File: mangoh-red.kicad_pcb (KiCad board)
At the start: 6 copper layers, 70 x 61.8 mm, 533 parts, among them CN1000 uFL, CN301 uFL, CN302 uFL, CN303 uFL, CN304 USB_A, CN305 USB_B_Micro, CN306 Conn_02x19_Counter_Clockwise, CN307 Conn_02x13_Odd_Even, CN310 Conn_02x03_Odd_Even, CN312 Conn_02x03_Odd_Even, CN500 JP036-RT3B4AB, CN801 USB_B_Micro, CN802 Conn_01x02, CN804 Conn_01x03, J200 CF3-Socket, SW401 Conn_02x08_Counter_Clockwise, U1000 MT7697, U1001 MX25L3233FM1I-08G_TR, U1004 SX1509BIULTRT, U1005 TPS61253YFFR, U1006 CP2130-F01-GM, U1007 24AA32AF-I-MNY, U1010 74LVC2G126HD4-7, U1020 74LVC2G126HD4-7, U301 FT230XQ-R, U302 TS3A5018RSVR, U304 74LVC2G126HD4-7, U306 FXMA108BQX, U307 FXMA108BQX, U337 FXMA108BQX, U400 NCP303LSN30T1G, U401 74AUP1G08GM, U402 74AUP1G08GM, U404 TCA9546APWR, U405 74AUP1G08GM, U500 WM8944BECS_R, U501 TS3A5018RSVR, U600 XC6223H29B9R-G, U610 TXS02612ZQSR, U701 USB3503A-1-GL-TR, U702 MIC2026-1YM, U704 BMI160, U705 BMP280, U706 PNJ4K01F, U800 BQ24296RGER, U801 LTC2942IDCB_TRMPBF, U900 TPS7A7300, U901 TPS62420DRC, U903 XC6221A182MR, Y1000 CT2520DB26000C0FZZA1

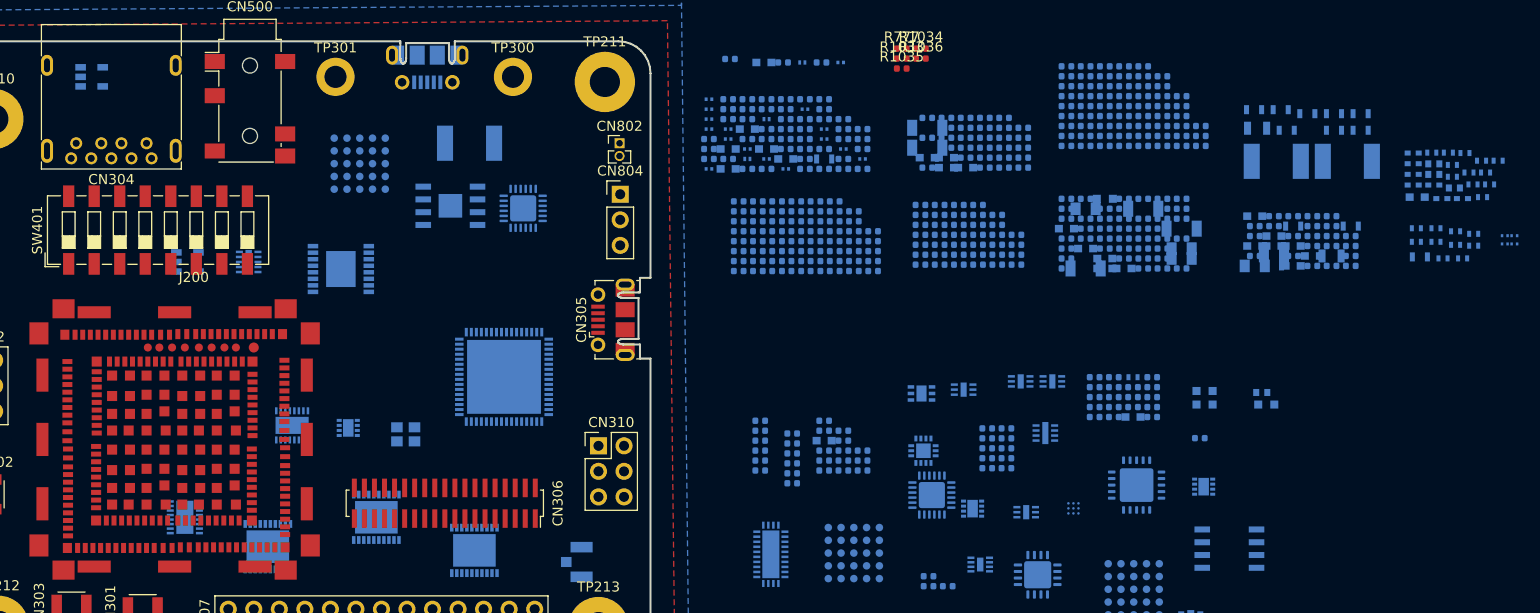
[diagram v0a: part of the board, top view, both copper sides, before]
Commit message: Refactor footprints and paths
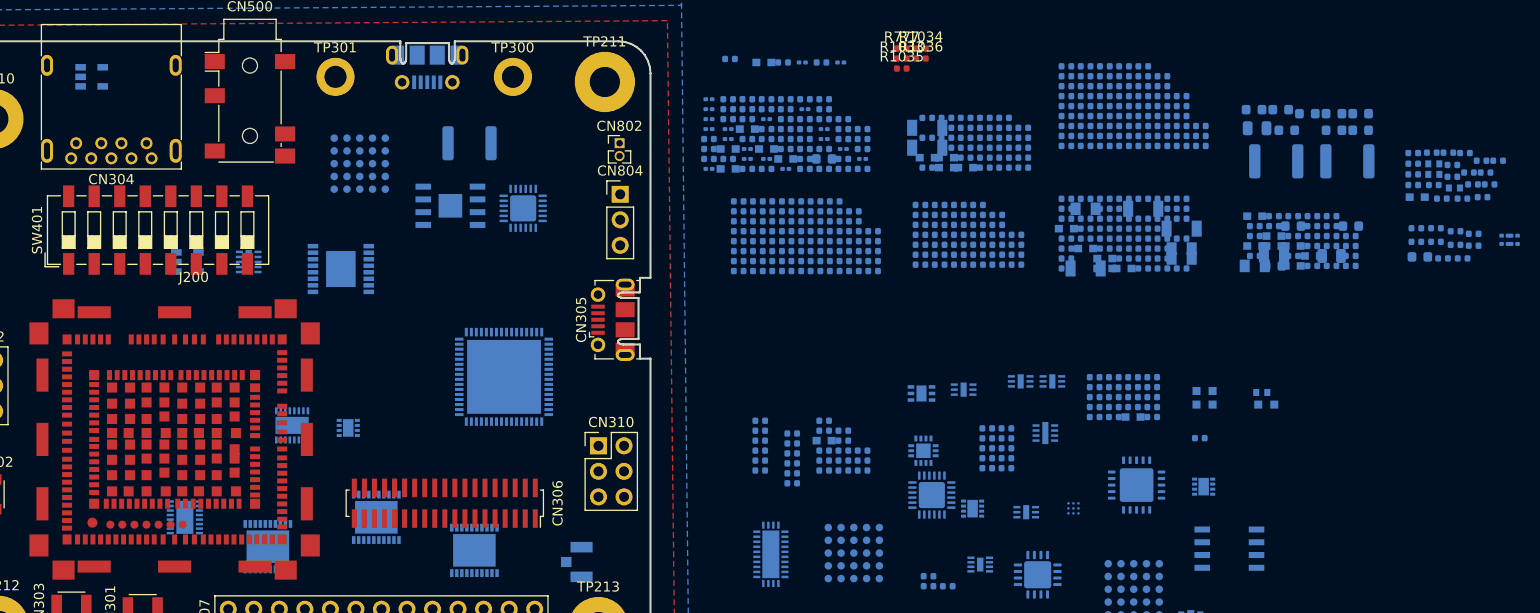
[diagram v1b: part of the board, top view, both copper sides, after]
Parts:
- removed Y1000: CT2520DB26000C0FZZA1, Crystal:Crystal_SMD_2520-4Pin_2.5x2.0mm
- C1005, C1010, C1013, C1022, C1023, C1024, C304, C308, C310, C311, C318, C515, C605, C801, C803, C807, C808, C809, C810, C818, C903, C924, C926, C927, C928: footprint Capacitors_SMD:C_0603 -> Capacitor_SMD:C_0603_1608Metric
- C1034, C1035, C1036, C1037, C1038, C1039, C1045, C1053, C1060, C1061, C1063, C1065, C1087, C1098, C1099, C1100: footprint Capacitors_SMD:C_0201 -> Capacitor_SMD:C_0201_0603Metric
- C302, C309, C908, C912, C920: footprint Capacitors_SMD:C_1206 -> Capacitor_SMD:C_1206_3216Metric
- C320, C321, C322, C355, C356, C360, C362: footprint Capacitors_SMD:C_0402 -> Capacitor_SMD:C_0402_1005Metric
- C800, C805, C906, C952, C955: footprint Capacitors_SMD:C_0805 -> Capacitor_SMD:C_0805_2012Metric
- C929: footprint LEDs:LED_0603 -> Capacitor_SMD:C_0402_1005Metric
- J200: footprint footprints:cf3 -> MangOH-Red:cf3
- L1001, L1002, L1026, L1087: footprint Inductors_SMD:L_0201 -> Inductor_SMD:L_0201_0603Metric
- L300, L500, L501, L502, L503, L504, L505, L506, L507: footprint Inductors_SMD:L_0402 -> Inductor_SMD:L_0402_1005Metric
- L508, L900, L901, L902, L903, L906, L907, L910, L912: footprint Inductors_SMD:L_0603 -> Inductor_SMD:L_0603_1608Metric
- L802, L904, L905: footprint Inductors_SMD:L_1812 -> Inductor_SMD:L_1812_4532Metric
- L911: footprint Inductors_SMD:L_0805 -> Inductor_SMD:L_0805_2012Metric
- R1006, R820, R826, R827: footprint Resistors_SMD:R_0603 -> Resistor_SMD:R_0603_1608Metric
- R1071, R1087, R1098: footprint Resistors_SMD:R_0201 -> Resistor_SMD:R_0201_0603Metric
- R310, R311, R312, R313, R340, R341, R343, R347, R361, R372, R378, R505, R506, R507: footprint Resistors_SMD:R_0402 -> Resistor_SMD:R_0402_1005Metric
- R828: footprint Resistors_SMD:R_0805 -> Resistor_SMD:R_0805_2012Metric

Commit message: Updates
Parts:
- added TP1000: TestPoint, MangOH-Red:Test_Point_Pad_d_0100, F.Cu at (269.6, 92.0)
- added TP1001: TestPoint, MangOH-Red:Test_Point_Pad_d_0100, F.Cu at (269.6, 89.9)
- added TP1002: TestPoint, MangOH-Red:Test_Point_Pad_d_0100, F.Cu at (267.5, 92.0)
- added TP1003: TestPoint, MangOH-Red:Test_Point_Pad_d_0100, F.Cu at (267.5, 89.9)
- added TP1004: TestPoint, MangOH-Red:Test_Point_Pad_d_0100, F.Cu at (265.5, 92.0)
- added TP1021: TestPoint, MangOH-Red:Test_Point_Pad_d_0100, F.Cu at (265.5, 89.9)
- added TP1022: TestPoint, MangOH-Red:Test_Point_Pad_d_0100, F.Cu at (263.4, 92.0)
- added TP1023: TestPoint, MangOH-Red:Test_Point_Pad_d_0100, F.Cu at (263.4, 89.9)
- added TP1024: TestPoint, MangOH-Red:Test_Point_Pad_d_0100, F.Cu at (261.4, 92.0)
- added TP1025: TestPoint, MangOH-Red:Test_Point_Pad_d_0100, F.Cu at (261.4, 89.9)
- added TP224: TestPoint, MangOH-Red:Test_Point_Pad_d_0100, F.Cu at (267.5, 98.8)
- added TP225: TestPoint, MangOH-Red:Test_Point_Pad_d_0100, F.Cu at (261.4, 98.8)
- added TP227: TestPoint, MangOH-Red:Test_Point_Pad_d_0100, F.Cu at (261.4, 100.9)
- added TP228: TestPoint, MangOH-Red:Test_Point_Pad_d_0100, F.Cu at (263.4, 98.8)
- added TP230: TestPoint, MangOH-Red:Test_Point_Pad_d_0100, F.Cu at (263.4, 100.9)
- added TP232: TestPoint, MangOH-Red:Test_Point_Pad_d_0100, F.Cu at (265.5, 98.8)
- added TP261: TestPoint, MangOH-Red:Test_Point_Pad_d_0100, F.Cu at (265.5, 100.9)
- added TP324: TestPoint, MangOH-Red:Test_Point_Pad_d_0100, F.Cu at (273.1, 98.8)
- added TP325: TestPoint, MangOH-Red:Test_Point_Pad_d_0100, F.Cu at (273.1, 100.9)
- added TP327: TestPoint, MangOH-Red:Test_Point_Pad_d_0100, F.Cu at (275.2, 98.8)
- added TP328: TestPoint, MangOH-Red:Test_Point_Pad_d_0100, F.Cu at (275.2, 100.9)
- added TP500: TestPoint, MangOH-Red:Test_Point_Pad_d_0035, F.Cu at (282.9, 96.6)
- added TP802: TestPoint, MangOH-Red:Test_Point_Pad_d_0100, F.Cu at (276.9, 92.0)
- added TP803: TestPoint, MangOH-Red:Test_Point_Pad_d_0100, F.Cu at (276.9, 89.9)
- added TP804: TestPoint, MangOH-Red:Test_Point_Pad_d_0100, F.Cu at (278.9, 89.9)
- added TP805: TestPoint, MangOH-Red:Test_Point_Pad_d_0100, F.Cu at (274.8, 89.9)
- added TP806: TestPoint, MangOH-Red:Test_Point_Pad_d_0100, F.Cu at (274.8, 92.0)
- added TP901: TestPoint, MangOH-Red:Test_Point_Pad_d_0100, F.Cu at (285.3, 89.9)
- added TP906: TestPoint, MangOH-Red:Test_Point_Pad_d_0100, F.Cu at (285.3, 92.0)
- added TP907: TestPoint, MangOH-Red:Test_Point_Pad_d_0100, F.Cu at (287.3, 89.9)
- added TP910: TestPoint, MangOH-Red:Test_Point_Pad_d_0100, F.Cu at (287.3, 92.0)
- TP210, TP211, TP212, TP213: footprint MountingHole:MountingHole_3mm_Pad -> MangOH-Red:Test_Point_Pad_d_0650
- TP300: value IOT_Mounting_Point_1 -> TestPoint; footprint MountingHole:MountingHole_2.2mm_M2_DIN965_Pad -> MangOH-Red:Test_Point_Pad_d_0100
- TP301: value IOT_Mounting_Point_2 -> TestPoint; footprint MountingHole:MountingHole_2.2mm_M2_DIN965_Pad -> MangOH-Red:Test_Point_Pad_d_0100
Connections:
- C1100 pad 1: Net-(ANT1000-Pad3) -> (no net)
- C230 pad 1: W_DISABLE_N -> (no net)
- C301 pad 2: RF_GPS -> (no net)
- CN305 pad 4: Net-(CN305-Pad4) -> (no net)
- CN306 pad 16: SPI1_CLK -> (no net)
- CN306 pad 17: SPI1_MISO -> (no net)
- CN306 pad 18: SPI1_MOSI -> (no net)
- CN306 pad 31: CARD_DETECT_IOT0 -> (no net)
- CN500 pad 2: Net-(CN500-Pad2) -> (no net)
- CN500 pad 3: Net-(CN500-Pad3) -> (no net)
- CN801 pad 2: Net-(CN801-Pad2) -> (no net)
- CN801 pad 3: Net-(CN801-Pad3) -> (no net)
- D410 pad 1: Net-(D410-Pad1) -> (no net)
- R216 pad 2: Net-(J200-Pad23) -> (no net)
- R217 pad 2: Net-(J200-Pad22) -> (no net)
- R222 pad 2: Net-(D200-Pad2) -> (no net)
- R223 pad 1: Net-(J200-Pad99) -> (no net)
- R224 pad 1: Net-(J200-Pad98) -> (no net)
- R230 pad 2: Net-(J200-Pad25) -> (no net)
- R238 pad 1: Net-(J200-Pad45) -> (no net)
- R252 pad 1: Net-(J200-Pad91) -> (no net)
- R287 pad 2: Net-(R287-Pad2) -> (no net)
- R306 pad 2: BAT_RTC -> (no net)
- R343 pad 2: Net-(Q405-Pad2) -> (no net)
- R345 pad 1: Net-(J200-Pad1) -> (no net)
- R346 pad 1: Net-(J200-Pad66) -> (no net)
- R347 pad 2: Net-(Q312-Pad2) -> (no net)
- R413 pad 1: Net-(D401-Pad2) -> (no net)
- R435 pad 1: Net-(D402-Pad2) -> (no net)
- R600 pad 2: Net-(CN600-PadT5) -> (no net)
- R604 pad 2: UIM1_DATA -> (no net)
- R611 pad 1: UIM2_DATA -> (no net)
- R611 pad 2: Net-(R611-Pad2) -> (no net)
- R645 pad 1: Net-(R645-Pad1) -> (no net)
- R645 pad 2: UIM2_CLK -> (no net)
- SW401 pad 1: PWR_ON -> (no net)
- U1000 pad 1: Net-(U1000-Pad1) -> (no net)
- U1000 pad 40: Net-(L1000-Pad1) -> (no net)
- U1000 pad 58: Net-(U1000-Pad58) -> (no net)
- U1000 pad 61: Net-(U1000-Pad61) -> (no net)
- U1004 pad 11: Net-(U1004-Pad11) -> (no net)
- U1006 pad 10: Net-(U1006-Pad10) -> (no net)
- U1006 pad 11: Net-(U1006-Pad11) -> (no net)
- U1006 pad 12: Net-(U1006-Pad12) -> (no net)
- U1006 pad 13: Net-(U1006-Pad13) -> (no net)
- U1006 pad 14: Net-(U1006-Pad14) -> (no net)
- U1006 pad 15: Net-(U1006-Pad15) -> (no net)
- U1006 pad 17: Net-(U1006-Pad17) -> (no net)
- U1006 pad 18: Net-(U1006-Pad18) -> (no net)
- U301 pad 11: Net-(U301-Pad11) -> (no net)
- U301 pad 12: Net-(U301-Pad12) -> (no net)
- U301 pad 14: Net-(U301-Pad14) -> (no net)
- U301 pad 5: Net-(U301-Pad5) -> (no net)
- U302 pad 1: Net-(U302-Pad1) -> (no net)
- U302 pad 11: Net-(U302-Pad11) -> (no net)
- U306 pad 14: WP_GPIO_7_lvl -> (no net)
- U306 pad 16: Net-(U306-Pad16) -> (no net)
- U306 pad 2: WP_GPIO_3 -> (no net)
- U306 pad 3: WP_GPIO_1 -> (no net)
- U306 pad 5: Net-(U306-Pad5) -> (no net)
- U306 pad 6: WP_GPIO_8 -> (no net)
- U306 pad 7: WP_GPIO_7 -> (no net)
- U307 pad 16: Net-(U307-Pad16) -> (no net)
- U307 pad 5: Net-(U307-Pad5) -> (no net)
- U337 pad 11: Net-(Q405-Pad6) -> (no net)
- U337 pad 12: Net-(U337-Pad12) -> (no net)
- U337 pad 13: Net-(U337-Pad13) -> (no net)
- U337 pad 14: Net-(U337-Pad14) -> (no net)
- U337 pad 4: UART1_CTS -> (no net)
- U337 pad 7: Net-(U337-Pad7) -> (no net)
- U337 pad 8: Net-(U337-Pad8) -> (no net)
- U337 pad 9: Net-(U337-Pad9) -> (no net)
- U400 pad 4: Net-(U400-Pad4) -> (no net)
- U401 pad 5: Net-(U401-Pad5) -> (no net)
- U402 pad 5: Net-(U402-Pad5) -> (no net)
- U405 pad 5: Net-(U405-Pad5) -> (no net)
- U500 pad C5: Net-(U500-PadC5) -> (no net)
- U500 pad D4: Net-(U500-PadD4) -> (no net)
- U500 pad D5: Net-(U500-PadD5) -> (no net)
- U500 pad E5: Net-(U500-PadE5) -> (no net)
- U610 pad A1: SD_D2 -> (no net)
- U610 pad B1: SD_D3 -> (no net)
- U610 pad C1: SD_CMD -> (no net)
- U610 pad D1: SD_D0 -> (no net)
- U610 pad D2: SD_CLK -> (no net)
- U610 pad E1: SD_D1 -> (no net)
- U701 pad B3: Net-(OSC1000-Pad3) -> (no net)
- U701 pad C4: Net-(U701-PadC4) -> (no net)
- U701 pad E1: HSIC_STRB -> (no net)
- U701 pad E2: HSIC_DATA -> (no net)
- U704 pad 10: Net-(U704-Pad10) -> (no net)
- U704 pad 11: Net-(U704-Pad11) -> (no net)
- U704 pad 2: Net-(U704-Pad2) -> (no net)
- U704 pad 3: Net-(U704-Pad3) -> (no net)
- U900 pad 10: Net-(U900-Pad10) -> (no net)
- U900 pad 11: Net-(U900-Pad11) -> (no net)
- U900 pad 12: Net-(U900-Pad12) -> (no net)
- U900 pad 4: Net-(U900-Pad4) -> (no net)
- U900 pad 5: Net-(U900-Pad5) -> (no net)
- U900 pad 6: Net-(U900-Pad6) -> (no net)
- U900 pad 7: Net-(U900-Pad7) -> (no net)
- U900 pad 9: Net-(U900-Pad9) -> (no net)
- U903 pad 4: Net-(U903-Pad4) -> (no net)

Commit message: Updating
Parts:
- added Q312: NSBC114YDP6T5G, MangOH-Red:SOT963_6P_0100x0080_0035CC, F.Cu at (210.4, 118.9)
- added Q400: NSBC114YDP6T5G, MangOH-Red:SOT963_6P_0100x0080_0035CC, F.Cu at (216.7, 118.9)
- added Q405: NSBC114YDP6T5G, MangOH-Red:SOT963_6P_0100x0080_0035CC, F.Cu at (212.0, 118.9)
- added Q600: PDTC115EM, MangOH-Red:DFN_3P_0060x0100_0035CC, F.Cu at (267.8, 111.8)
- added TP904: TestPoint, MangOH-Red:Test_Point_Pad_d_0200, F.Cu at (259.1, 111.8)
- added TP905: TestPoint, MangOH-Red:Test_Point_Pad_d_0200, F.Cu at (261.7, 111.8)
- J200: footprint MangOH-Red:cf3 -> MangOH-Red:CF3-Socket
- R251, R291, R632: value 100k (1%) -> 100k
- R600: value 33 (5%) -> 33
- R723: value 10K 1% -> 10K
- R900, R906: value 33k (1%) -> 33k
- R902, R903: value 0 (0%) -> 0
- R905: value 220k (1%) -> 220k
- U1000: footprint Housings_DFN_QFN:QFN-64-1EP_9x9mm_Pitch0.5mm -> MangOH-Red:QFN_68P_0800x0800_SLUG_0550x0550_0040CC
- U1001: footprint Package_SO:SOIC-8_3.9x4.9mm_P1.27mm -> MangOH-Red:SOIC_8P_0490x0390_0127CC
- U1004: footprint Housings_DFN_QFN:QFN-28-1EP_3x6mm_Pitch0.5mm -> MangOH-Red:QFN_28P_0400x0400_SLUG_0265x0265_0040CC
- U1005: footprint Package_BGA:BGA-9_1.6x1.6mm_Layout3x3_P0.5mm -> MangOH-Red:BGA_9P_0130x0120_0040CC_0023PD
- U1006, U800: footprint Package_DFN_QFN:QFN-24-1EP_4x4mm_P0.5mm_EP2.6x2.6mm -> MangOH-Red:QFN_24P_0400x0400_SLUG_0270x0270_0050CC
- U1007: footprint Package_DFN_QFN:DFN-8-1EP_2x3mm_P0.5mm_EP0.61x2.2mm -> MangOH-Red:DFN_8P_0200x0300_SLUG_0140x0140_0050CC
- U1010, U1020: footprint Package_DFN_QFN:DFN-8-1EP_2x2mm_P0.5mm_EP1.05x1.75mm -> MangOH-Red:DFN_8P_0200x0100_0050CC
- U301: footprint Package_DFN_QFN:QFN-16-1EP_4x4mm_P0.65mm_EP2.7x2.7mm -> MangOH-Red:QFN_16P_0400x0400_SLUG_0210x0210_0065CC
- U302, U501: footprint Package_DFN_QFN:DFN-16-1EP_3x4mm_P0.45mm_EP1.7x3.3mm -> MangOH-Red:QFN_14P_0250x0300_0050CC
- U304: footprint Housings_DFN_QFN:DFN-8-1EP_2x2mm_Pitch0.45mm -> MangOH-Red:DFN_8P_0200x0100_0050CC
- U306, U307, U337: footprint Package_DFN_QFN:DFN-20-1EP_5x6mm_P0.5mm_EP3.24x4.24mm -> MangOH-Red:QFN_20P_0250x0450_SLUG_0115x0315_0050CC
- U400, U903: footprint Package_TO_SOT_SMD:SOT-23-5 -> MangOH-Red:SOT23_5P_0300x0160_0095CC
- U404: footprint Package_SO:TSSOP-16-1EP_4.4x5mm_P0.65mm -> MangOH-Red:TSSOP_16P_0500x0440_0065CC
- U500: footprint Package_BGA:BGA-25_6.35x6.35mm_Layout5x5_P1.27mm -> MangOH-Red:BGA_25P_0241x0241_0050CC_0030PD
- U600: footprint Package_DFN_QFN:AMS_QFN-4-1EP_2x2mm_P0.95mm_EP0.7x1.6mm -> MangOH-Red:DFN_4P_0100x0100_SLUG_ROTATED_45DEG_0042x0042_0065CC
- U610: footprint Package_BGA:BGA-25_6.35x6.35mm_Layout5x5_P1.27mm -> MangOH-Red:BGA_24P_0300x0300_0050CC_0030PD
- U701: footprint Housings_BGA:BGA-25_5x5_6.35x6.35mm_Pitch1.27mm -> MangOH-Red:BGA_25P_0200x0200_0040CC_0030PD
- U702: footprint Package_SO:SOIC-8-1EP_3.9x4.9mm_P1.27mm_EP2.35x2.35mm -> MangOH-Red:SOIC_8P_0490x0390_0127CC
- U704: footprint Package_DFN_QFN:WQFN-14-1EP_2.5x2.5mm_P0.5mm_EP1.45x1.45mm -> MangOH-Red:QFN_14P_0250x0300_0050CC
- U705: footprint Package_DFN_QFN:DFN-8-1EP_2x2mm_P0.5mm_EP1.05x1.75mm -> MangOH-Red:DFN_8P_0250x0200_0065CC
- U801: footprint Package_DFN_QFN:DFN-6-1EP_2x2mm_P0.65mm_EP1x1.6mm -> MangOH-Red:DFN_6P_0200x0300_SLUG_0135x0165_0050CC
- U901: footprint Housings_DFN_QFN:DFN-10-1EP_2x3mm_Pitch0.5mm -> MangOH-Red:DFN_10P_0300x0300_SLUG_0240x0165_0050CC_TI_POWERPAD
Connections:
- CN306 pad 35: PCM_SYNC_IOT -> (no net)
- R343 pad 2: (no net) -> Net-(Q405-Pad2)
- R347 pad 2: (no net) -> Net-(Q312-Pad2)
- U307 pad 13: /3. RF, USB, IOT connectors/UART2_RTS_3V3 -> (no net)
- U337 pad 11: (no net) -> Net-(Q405-Pad6)

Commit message: Updates
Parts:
- moved C801 125.7 mm to (128.2, 73.7)
- moved L1001 105.0 mm to (175.9, 107.3), turned to 135 degrees
- moved L1002 103.2 mm to (177.2, 106.0), turned to 135 degrees
- moved R345 101.4 mm to (125.7, 61.6), turned to 90 degrees
- moved L1087 99.9 mm to (181.6, 111.8), turned to 45 degrees
- moved U402 89.2 mm to (146.1, 65.4)
- moved R222 79.7 mm to (148.0, 61.0), turned to 90 degrees
- moved R442 74.8 mm to (135.9, 66.7), turned to 90 degrees
- moved R441 74.4 mm to (138.4, 65.4), turned to 90 degrees
- moved C401 71.7 mm to (129.5, 64.1)
- moved R455 68.8 mm to (139.7, 67.9)
- moved R410 66.4 mm to (141.0, 65.4), turned to 90 degrees
- moved C400 65.8 mm to (135.9, 64.1)
- moved R413 65.7 mm to (135.9, 60.3), turned to 90 degrees
- moved R430 63.9 mm to (179.1, 130.2), turned to 90 degrees
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
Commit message: Add SnapEDA footprint and symbol for WP Snap In Base socket. Per SnapEDA's license, these parts are licensed as follows: "Creative Commons Attribution-ShareAlike 4.0 International License (CC BY-SA) with the Design Exception 1.0." The text of the Design Exception reads as follows: "You have permission to propagate a work of a design, design file(s) and/or manufactured board(s) formed by combining CAD symbols and footprints provided by SnapEDA, even if such propagation would otherwise violate the terms of CC BY-SA. You may then convey such a combination under terms of your choice."
For full license details see:  https://www.snapeda.com/about/FAQ/#faq
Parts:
- removed C1000, C1003, C1007, C1012, C1014, C1020, C322, C360, C362, C405, C406, C517, C518, C520, C624, C702, C715, C720, C721, C722, C723, C725, C900, C902, C905, C907, C915, C916, C917, C918, C919, C921, C933: 100n, Capacitor_SMD:C_0402_1005Metric
- removed C1001, C1004: 470n, Capacitor_SMD:C_0402_1005Metric
- removed C1002, C1027, C1028, C1029, C1031: 10p, Capacitor_SMD:C_0402_1005Metric
- removed C1005, C1013, C818, C903: 10u, Capacitor_SMD:C_0603_1608Metric
- removed C1006, C1019, C1026, C1030, C1033, C500, C501, C502, C505, C506, C510, C511, C516: 100p, Capacitor_SMD:C_0402_1005Metric
- removed C1008, C1009, C1025, C509, C512, C513, C514, C519, C788: 4.7u, Capacitor_SMD:C_0402_1005Metric
- removed C1010, C1022, C1023, C1024, C515: 2.2u, Capacitor_SMD:C_0603_1608Metric
- removed C1011, C1016, C1018, C1021, C1032, C503, C504: 1u, Capacitor_SMD:C_0402_1005Metric
- removed C1015: 470p, Capacitor_SMD:C_0402_1005Metric
- removed C1017, C812: 10u, Capacitor_SMD:C_0402_1005Metric
- removed C1034: 1p, Capacitor_SMD:C_0201_0603Metric
- removed C1035, C1036, C1039, C1053, C1065: 1.5p, Capacitor_SMD:C_0201_0603Metric
- removed C1037, C1038: 1.8p, Capacitor_SMD:C_0201_0603Metric
- removed C1045, C1063, C1098, C1099, C1100: 10p, Capacitor_SMD:C_0201_0603Metric
- removed C1060: 2.7p, Capacitor_SMD:C_0201_0603Metric
- removed C1061: 100p, Capacitor_SMD:C_0201_0603Metric
- removed C1087: 2.2p, Capacitor_SMD:C_0201_0603Metric
- removed C250: 1n, Capacitor_SMD:C_0402_1005Metric
- removed C507, C508: 22p, Capacitor_SMD:C_0402_1005Metric
- removed C909: 47n, Capacitor_SMD:C_0402_1005Metric
- removed C911: 10n, Capacitor_SMD:C_0402_1005Metric
- removed C920: 47u, Capacitor_SMD:C_1206_3216Metric
- removed C922: 1.5m, Capacitor_SMD:C_0402_1005Metric
- removed CN1000: uFL, Connector_Coaxial:U.FL_Hirose_U.FL-R-SMT-1_Vertical
- removed CN306: Conn_02x19_Counter_Clockwise, Connector_PinSocket_1.00mm:PinSocket_2x19_P1.00mm_Vertical_SMD
- removed CN310: Conn_02x03_Odd_Even, Connector_PinHeader_2.54mm:PinHeader_2x03_P2.54mm_Vertical
- removed CN500: JP036-RT3B4AB, Connector_Audio:Jack_3.5mm_PJ311_Horizontal
- removed L1001, L1002: 1.2n, Inductor_SMD:L_0201_0603Metric
- removed L1026: 2.2n, Inductor_SMD:L_0201_0603Metric
- removed L1087: 2.4n, Inductor_SMD:L_0201_0603Metric
- removed L500, L501, L504, L505, L506, L507: 0, Inductor_SMD:L_0402_1005Metric
- removed L502, L503: 22n, Inductor_SMD:L_0402_1005Metric
- removed L508, L900: 0, Inductor_SMD:L_0603_1608Metric
- removed Q405: NSBC114YDP6T5G, MangOH-Red:SOT963_6P_0100x0080_0035CC
- removed R1000, R1001, R1002, R1003, R1004, R1005, R1051, R1077, R1079, R1088, R313, R372, R376, R377, R379, R388, R411, R422, R508, R509, R520, R671, R703, R704, R715, R722, R726, R727, R731, R744, R777, R781, R804, R805, R807, R808, R812: 10k, Resistor_SMD:R_0402_1005Metric
- removed R1006, R820, R826, R827: 0, Resistor_SMD:R_0603_1608Metric
- removed R1007: 36, Resistor_SMD:R_0402_1005Metric
- removed R1030, R1031, R1032, R1069, R735: 10K, Resistor_SMD:R_0402_1005Metric
- removed R1033, R1034, R401, R403, R456, R457, R476: 47k, Resistor_SMD:R_0402_1005Metric
- removed R1035, R1036: 33, Resistor_SMD:R_0402_1005Metric
- removed R1068, R1078, R1091, R1092, R216, R217, R223, R224, R230, R238, R252, R255, R267, R278, R279, R309, R340, R341, R343, R344, R345, R346, R347, R348, R350, R363, R365, R366, R367, R368, R369, R370, R371, R373, R374, R375, R382, R392, R400, R416, R417, R418, R426, R427, R439, R440, R441, R442, R460, R461, R467, R475, R495, R505, R506, R507, R515, R516, R610, R611, R612, R645, R725, R732, R733, R736, R737, R739, R753, R754, R755, R778, R782, R785, R786, R793, R794, R795, R796, R798, R825, R902, R903, R940, R970: 0, Resistor_SMD:R_0402_1005Metric
- removed R1071, R1087: 10k, Resistor_SMD:R_0201_0603Metric
- removed R1098: 2.7p, Resistor_SMD:R_0201_0603Metric
- removed R251, R291, R402: 100k, Resistor_SMD:R_0402_1005Metric
- removed R361: 820k, Resistor_SMD:R_0402_1005Metric
- removed R409, R458: 330, Resistor_SMD:R_0402_1005Metric
- removed R445: 100, Resistor_SMD:R_0402_1005Metric
- removed R466: 4.7k, Resistor_SMD:R_0402_1005Metric
- removed R500, R501: 2.2k, Resistor_SMD:R_0402_1005Metric
- removed R504: 20K, Resistor_SMD:R_0402_1005Metric
- removed R813: 15k, Resistor_SMD:R_0402_1005Metric
- removed R900, R906: 33k, Resistor_SMD:R_0402_1005Metric
- removed R901: R, Resistor_SMD:R_0402_1005Metric
- removed R905: 220k, Resistor_SMD:R_0402_1005Metric
- removed TP1000, TP1001, TP1002, TP1003, TP1004, TP1021, TP1022, TP1023, TP1024, TP1025, TP324, TP325, TP327, TP328: TestPoint, MangOH-Red:Test_Point_Pad_d_0100
- removed TP500: TestPoint, MangOH-Red:Test_Point_Pad_d_0035
- removed U1000: MT7697, MangOH-Red:QFN_68P_0800x0800_SLUG_0550x0550_0040CC
- removed U1001: MX25L3233FM1I-08G_TR, MangOH-Red:SOIC_8P_0490x0390_0127CC
- removed U1006: CP2130-F01-GM, MangOH-Red:QFN_24P_0400x0400_SLUG_0270x0270_0050CC
- removed U1010, U1020, U304: 74LVC2G126HD4-7, MangOH-Red:DFN_8P_0200x0100_0050CC
- removed U302, U501: TS3A5018RSVR, MangOH-Red:QFN_14P_0250x0300_0050CC
- removed U337: FXMA108BQX, MangOH-Red:QFN_20P_0250x0450_SLUG_0115x0315_0050CC
- removed U401, U405: 74AUP1G08GM, Package_DFN_QFN:DFN-6-1EP_2x2mm_P0.5mm_EP0.61x1.42mm
- removed U500: WM8944BECS_R, MangOH-Red:BGA_25P_0241x0241_0050CC_0030PD
- removed U705: BMP280, MangOH-Red:DFN_8P_0250x0200_0065CC
- removed U706: PNJ4K01F, Package_DFN_QFN:DFN-6-1EP_2x2mm_P0.5mm_EP0.61x1.42mm
- removed U900: TPS7A7300, Package_DFN_QFN:QFN-20-1EP_5x5mm_P0.65mm_EP3.35x3.35mm
- moved J200 56.3 mm to (162.1, 148.0)
- moved C213 3.76 mm to (215.4, 81.3)
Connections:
- C230 pad 1: (no net) -> W_DISABLE_N
- C301 pad 2: (no net) -> RF_GPS
- C400 pad 1: RESET_IN -> Power_Fail_Indicator
- CN305 pad 4: (no net) -> Net-(CN305-Pad4)
- CN307 pad 12: Net-(CN307-Pad12) -> PWM_OUT_3V3
- CN307 pad 2: Net-(CN307-Pad2) -> VCC
- CN307 pad 3: Net-(CN307-Pad3) -> SDA_EXP
- CN307 pad 4: Net-(CN307-Pad2) -> VCC
- CN307 pad 5: Net-(CN307-Pad5) -> SCL_EXP
- CN312 pad 1: WP_GPIO_4_Wakeable -> SENSOR_INT1
- CN312 pad 3: WP_GPIO_5_Wakeable -> SENSOR_INT2
- CN312 pad 4: Net-(CN312-Pad4) -> ADC1
- CN312 pad 5: RFU_PIN -> ADC2
- CN801 pad 2: (no net) -> Net-(CN801-Pad2)
- CN801 pad 3: (no net) -> Net-(CN801-Pad3)
- D400 pad 1: RESET_IN -> Power_Fail_Indicator
- D410 pad 1: (no net) -> Net-(D410-Pad1)
- Q312 pad 1: GND -> (no net)
- Q312 pad 2: Net-(Q312-Pad2) -> (no net)
- Q312 pad 5: Net-(Q312-Pad5) -> VCC
- Q312 pad 6: Net-(Q312-Pad6) -> (no net)
- Q400 pad 2: LED_CARD_DETECT_IOT0 -> BattChrgr_INT_N
- Q400 pad 3: (no net) -> Net-(D402-Pad1)
- Q400 pad 5: (no net) -> 2G_TX_ON
- Q400 pad 6: (no net) -> Net-(D401-Pad1)
- R222 pad 2: (no net) -> Net-(D200-Pad2)
- R287 pad 2: (no net) -> Net-(R287-Pad2)
- R306 pad 2: (no net) -> BAT_RTC
- R410 pad 2: RESET_IN -> Power_Fail_Indicator
- R413 pad 1: (no net) -> Net-(D401-Pad2)
- R429 pad 2: Net-(R427-Pad1) -> Charger_I2C_CLK
- R431 pad 2: Net-(R426-Pad1) -> Charger_I2C_DATA
- R435 pad 1: (no net) -> Net-(D402-Pad2)
- R462 pad 1: WIFI_I2C0_DATA -> GPIO1|I2C1_CLK
- R463 pad 1: WIFI_I2C0_CLK -> GPIO1|I2C1_CLK
- R600 pad 2: (no net) -> Net-(CN600-PadT5)
- R604 pad 2: (no net) -> UIM1_DATA
- SW401 pad 1: (no net) -> PWR_ON
- SW401 pad 13: Net-(R495-Pad2) -> VCC
- TP224 pad 1: (no net) -> Net-(J200-Pad155)
- TP225 pad 1: (no net) -> Net-(J200-Pad153)
- TP227 pad 1: (no net) -> Net-(J200-Pad156)
- TP228 pad 1: (no net) -> Net-(J200-Pad154)
- TP230 pad 1: (no net) -> Net-(J200-Pad152)
- TP261 pad 1: (no net) -> Net-(J200-Pad110)
- TP803 pad 1: Net-(R827-Pad2) -> VCC
- U1004 pad 11: (no net) -> Net-(U1004-Pad11)
- U1004 pad 13: Net-(R785-Pad2) -> BattChrgr_INT_N
- U1004 pad 14: Net-(R755-Pad2) -> SDIO_SEL
- U1004 pad 23: GPIO_IOT0_RESET -> System_reset
- U1004 pad 6: Net-(R753-Pad2) -> MTK_TO_WP_UART_EN
- U301 pad 11: (no net) -> Net-(U301-Pad11)
- U301 pad 12: (no net) -> Net-(U301-Pad12)
- U301 pad 14: (no net) -> Net-(U301-Pad14)
- U301 pad 5: (no net) -> Net-(U301-Pad5)
- U306 pad 14: (no net) -> WP_GPIO_7_lvl
- U306 pad 16: (no net) -> Net-(U306-Pad16)
- U306 pad 2: (no net) -> WP_GPIO_3
- U306 pad 3: (no net) -> WP_GPIO_1
- U306 pad 5: (no net) -> Net-(U306-Pad5)
- U306 pad 6: (no net) -> WP_GPIO_8
- U306 pad 7: (no net) -> WP_GPIO_7
- U307 pad 11: Net-(Q312-Pad6) -> GND
- U307 pad 12: /3. RF, USB, IOT connectors/UART2_CTS_3V3 -> /3. RF, USB, IOT connectors/CTS_FTDI
- U307 pad 13: (no net) -> /3. RF, USB, IOT connectors/RTS_FTDI
- U307 pad 14: /3. RF, USB, IOT connectors/UART2_RX_3V3 -> /3. RF, USB, IOT connectors/RX_FTDI
- U307 pad 15: WIFI_UART0_TX -> /3. RF, USB, IOT connectors/TX_FTDI
- U307 pad 16: (no net) -> Net-(U307-Pad16)
- U307 pad 17: RESET_WIFI_3V3 -> Net-(U307-Pad17)
- U307 pad 4: RESET_WIFI_1V8 -> Net-(U307-Pad4)
- U307 pad 5: (no net) -> Net-(U307-Pad5)
- U400 pad 1: Net-(R441-Pad1) -> Power_Fail_Indicator
- U400 pad 2: Net-(R400-Pad1) -> VCC
- U400 pad 4: (no net) -> Net-(U400-Pad4)
- U402 pad 1: RESET_IN -> Power_Fail_Indicator
- U402 pad 4: GPIO_IOT0_RESET -> System_reset
- U402 pad 5: (no net) -> Net-(U402-Pad5)
- U404 pad 1: Net-(R417-Pad2) -> VCC
- U404 pad 13: Net-(R418-Pad2) -> GND
- U404 pad 2: Net-(R416-Pad2) -> GND
- U404 pad 3: Net-(R466-Pad2) -> System_reset
- U404 pad 6: Net-(R427-Pad1) -> Charger_I2C_CLK
- U404 pad 7: Net-(R426-Pad1) -> Charger_I2C_DATA
- U610 pad A1: (no net) -> SD_D2
- U610 pad B1: (no net) -> SD_D3
- U610 pad C1: (no net) -> SD_CMD
- U610 pad C4: Net-(R610-Pad2) -> VCC
- U610 pad D1: (no net) -> SD_D0
- U610 pad D2: (no net) -> SD_CLK
- U610 pad E1: (no net) -> SD_D1
- U701 pad B3: (no net) -> Net-(OSC1000-Pad3)
- U701 pad C4: (no net) -> Net-(U701-PadC4)
- U701 pad E1: (no net) -> HSIC_STRB
- U701 pad E2: (no net) -> HSIC_DATA
- U701 pad E3: GPIO_IOT0_RESET -> System_reset
- U702 pad 2: Net-(R725-Pad2) -> OSC_N
- U702 pad 3: Net-(R725-Pad2) -> OSC_N
- U704 pad 10: (no net) -> Net-(U704-Pad10)
- U704 pad 11: (no net) -> Net-(U704-Pad11)
- U704 pad 13: Net-(R793-Pad2) -> GPIO1|I2C1_CLK
- U704 pad 14: Net-(R794-Pad2) -> GPIO1|I2C1_CLK
- U704 pad 2: (no net) -> Net-(U704-Pad2)
- U704 pad 3: (no net) -> Net-(U704-Pad3)
- U704 pad 4: Net-(R732-Pad2) -> SENSOR_INT1
- U704 pad 9: Net-(R733-Pad2) -> SENSOR_INT2
- U903 pad 4: (no net) -> Net-(U903-Pad4)
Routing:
- net CONS_DIR: track 0.00 -> 0.60 mm
